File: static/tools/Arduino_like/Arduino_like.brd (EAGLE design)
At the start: 63.5 x 37.8 mm, 18 parts, among them IC1 MEGA8-P

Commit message: [Arduino_like] modify board.
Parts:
- moved C1-REGULATOR 1.91 mm to (8.26, 12.7)
- moved C2-REGULATOR 1.91 mm to (8.26, 27.9)
- moved IC2 1.91 mm to (4.45, 20.3)
- moved JP1 1.42 mm to (37.5, 34.3)
- moved CAVALIER_LED 1.27 mm to (55.9, 19.1)
- moved ALIM 0.64 mm to (4.45, 7.62)
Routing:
- net N$5: track 24.7 -> 27.5 mm
- net VCC: track 69.6 -> 67.7 mm
- net N$3: track 22.6 -> 24.2 mm
- net N$7: track 8.89 -> 10.4 mm
- net GND: track 146.4 -> 147.6 mm
- net N$4: track 53.9 -> 54.5 mm
- net N$26: track 3.07 -> 3.59 mm
- net N$6: track 9.42 -> 9.94 mm
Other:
- board size 63.5 x 37.8 mm -> 63.5 x 39 mm

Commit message: [Arduino_like] adds GND, VCC and AREF pins.
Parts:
- added JP6: (no value), pinhead:1X03
- moved CAVALIER_VCC 3.70 mm to (23.5, 36.2)
- moved JP1 2.54 mm to (37.5, 36.8)
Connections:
- new net N$29: IC1.21, JP6.1
- net GND: now also JP6.3
- net VCC: now also JP6.2
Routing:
- net N$29: track 0.00 -> 40.7 mm, vias 0 -> 1
- net VCC: track 67.7 -> 80.1 mm
- net GND: track 147.6 -> 158.2 mm
- net N$28: track 5.08 -> 12.7 mm
- net N$15: track 4.97 -> 8.41 mm
- net N$7: track 10.4 -> 13.0 mm
- net N$5: track 27.5 -> 30.0 mm
- net N$3: track 24.2 -> 26.7 mm
- net N$4: track 54.5 -> 57.1 mm
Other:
- board size 63.5 x 39 mm -> 62.2 x 42.9 mm
- board text added: "AREF"
- board text added: "GND"
- board text added: "VCC"

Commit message: [Arduino like] move on 0.1 inch grid.
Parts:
- moved CAVALIER_VCC 5.85 mm to (17.8, 37.5)
- moved JP1 5.72 mm to (31.8, 36.8)
- moved C1-REGULATOR 2.54 mm to (5.71, 12.7)
- moved C2-REGULATOR 2.54 mm to (5.71, 27.9)
- moved ALIM 2.54 mm to (1.91, 7.62)
- moved IC2 2.54 mm to (1.91, 20.3)
- moved C1-CRYSTAL 2.54 mm to (29.2, 7.62)
- moved C2-CRYSTAL 2.54 mm to (39.4, 7.62)
- moved CAVALIER_LED 2.54 mm to (53.3, 19.1)
- moved IC1 2.54 mm to (31.8, 19.1)
- moved JP2 2.54 mm to (21.6, 27.9)
- moved JP3 2.54 mm to (43.2, 27.9)
- moved JP4 2.54 mm to (20.3, 10.2)
- moved JP5 2.54 mm to (47.0, 10.2)
- moved LED1 2.54 mm to (57.1, 19.1)
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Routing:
- net N$34: track 0.00 -> 12.7 mm
- net N$31: track 0.00 -> 10.2 mm
- net N$40: track 0.00 -> 7.62 mm
- net N$32: track 0.00 -> 7.62 mm
- net N$37: track 0.00 -> 7.62 mm
- net N$35: track 0.00 -> 7.62 mm
- net N$30: track 0.00 -> 7.62 mm
- net N$41: track 0.00 -> 6.35 mm
- net N$38: track 0.00 -> 6.35 mm
- net N$36: track 0.00 -> 6.35 mm
- net N$33: track 0.00 -> 6.35 mm
- net N$39: track 0.00 -> 6.35 mm
- net GND: track 158.2 -> 163.1 mm
- net N$7: track 13.0 -> 14.3 mm
- net N$5: track 30.0 -> 31.3 mm
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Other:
- board size 62.2 x 42.9 mm -> 62.2 x 40.9 mm
- board text added: "BOTTOM"
- board text added: "TOP"
- board text added: "by Fab@ENAC-2015"

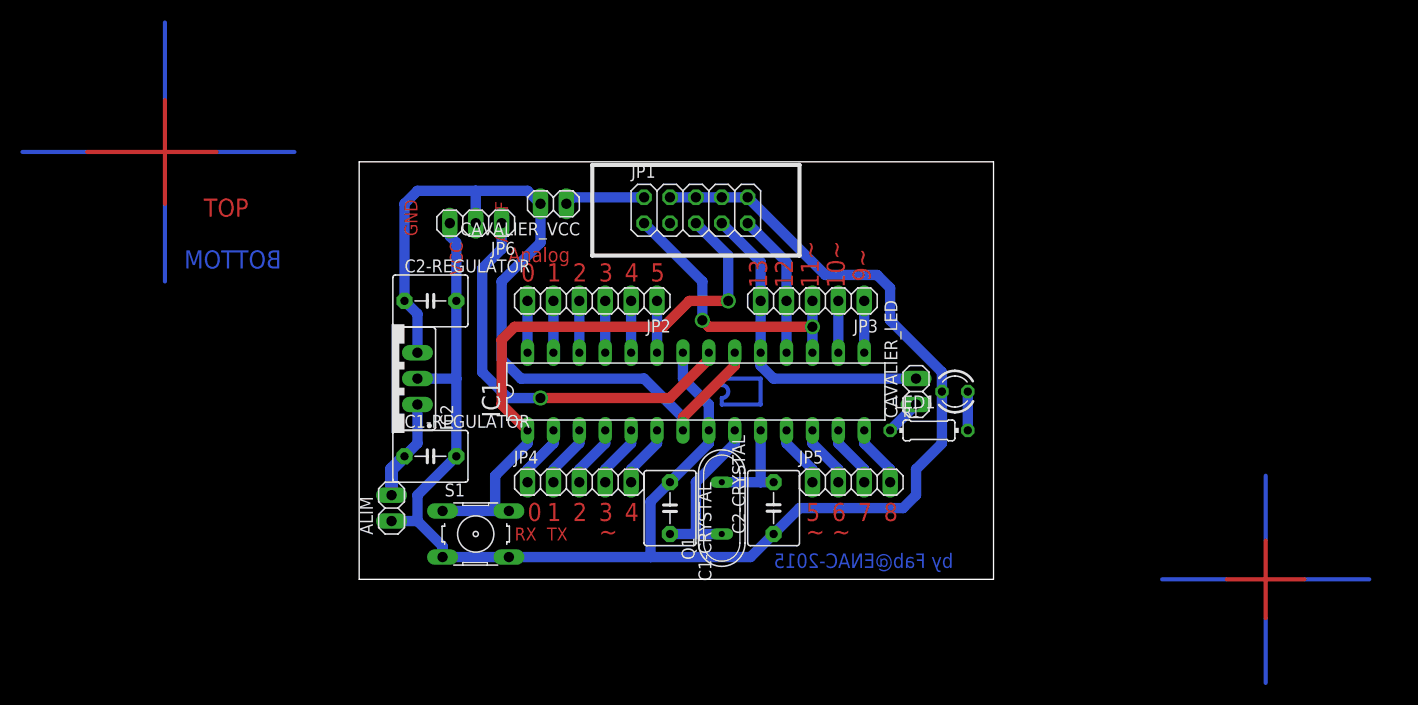
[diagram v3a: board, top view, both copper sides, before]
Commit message: [Arduino like] align pins.
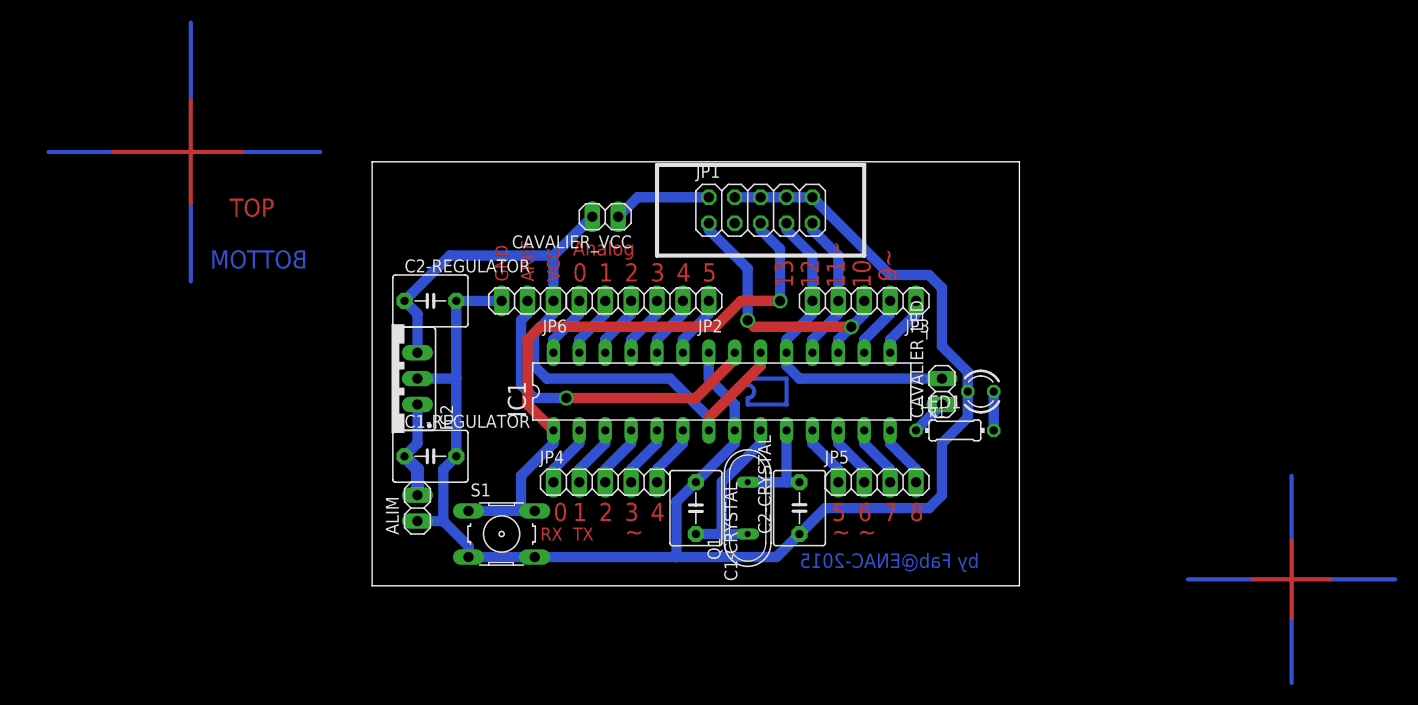
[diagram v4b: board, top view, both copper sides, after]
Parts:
- moved JP6 9.16 mm to (15.2, 27.9)
- moved JP1 6.35 mm to (38.1, 36.8)
- moved CAVALIER_VCC 5.24 mm to (22.9, 36.2)
- moved JP2 5.08 mm to (26.7, 27.9)
- moved JP3 5.08 mm to (48.3, 27.9)
- moved ALIM 2.54 mm to (4.45, 7.62)
- moved C1-CRYSTAL 2.54 mm to (31.8, 7.62)
- moved C2-CRYSTAL 2.54 mm to (41.9, 7.62)
- moved CAVALIER_LED 2.54 mm to (55.9, 19.1)
- moved IC1 2.54 mm to (34.3, 19.1)
- moved JP4 2.54 mm to (22.9, 10.2)
- moved JP5 2.54 mm to (49.5, 10.2)
- moved LED1 2.54 mm to (59.7, 19.1)
- moved Q1 2.54 mm to (36.8, 7.62)
- moved R1 2.54 mm to (57.1, 15.2)
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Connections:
- removed net N$29: IC1.21, JP6.1
- new net AREF: IC1.21, JP6.2
- net VCC: now also JP6.1; no longer JP6.2
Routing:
- net N$29: track 40.9 -> 0.00 mm, vias 1 -> 0
- net AREF: track 0.00 -> 32.2 mm, vias 0 -> 1
- net VCC: track 80.7 -> 69.3 mm
- net GND: track 163.1 -> 156.3 mm
- net N$4: track 58.4 -> 60.4 mm
- net N$15: track 7.88 -> 9.68 mm
- net N$24: track 5.08 -> 6.13 mm
- net N$8: track 5.08 -> 6.13 mm
- net N$10: track 5.08 -> 6.13 mm
- net N$9: track 5.08 -> 6.13 mm
- net N$25: track 5.08 -> 6.13 mm
- net N$13: track 5.08 -> 6.13 mm
- net N$12: track 5.08 -> 6.13 mm
- net N$11: track 5.08 -> 6.13 mm
- net N$7: track 14.3 -> 14.8 mm
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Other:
- board size 62.2 x 40.9 mm -> 63.5 x 41.6 mm

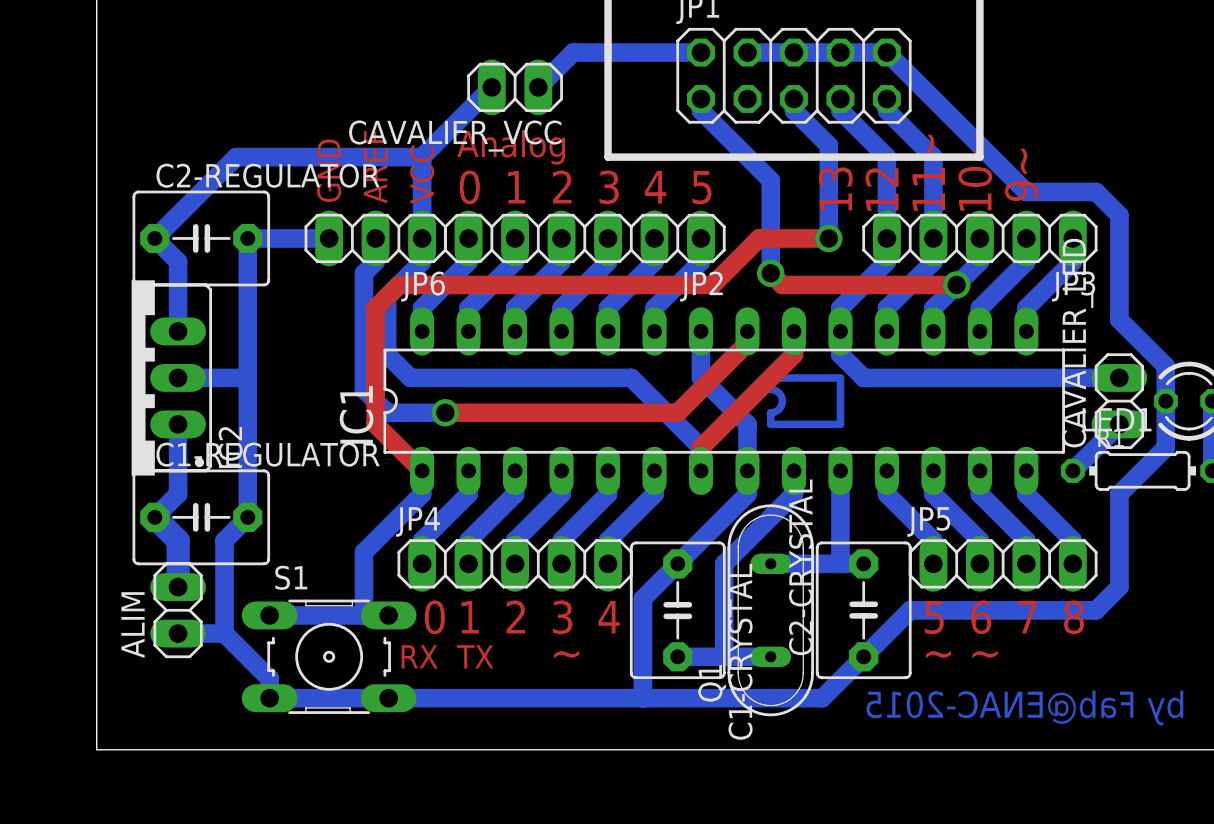
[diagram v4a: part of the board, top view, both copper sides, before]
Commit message: [Arduino_like] align power.
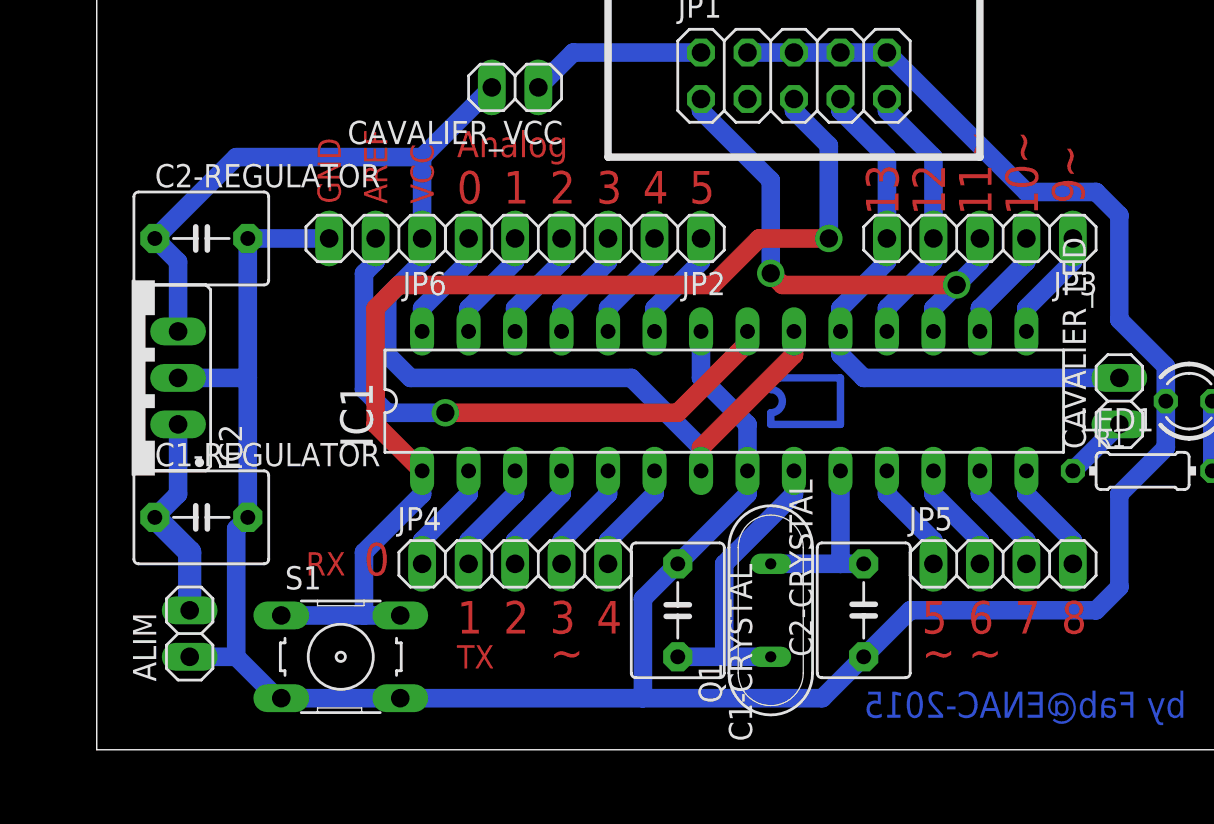
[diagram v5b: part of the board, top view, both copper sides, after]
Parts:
- moved ALIM 1.42 mm to (5.08, 6.35)
- moved S1 0.64 mm to (13.3, 5.08)
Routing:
- net N$6: track 9.94 -> 11.5 mm
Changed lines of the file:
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@@
 <layer number="19" name="Unrouted" color="6" fill="1" visible="yes" active="yes"/>
 <layer number="20" name="Dimension" color="15" fill="1" visible="yes" active="yes"/>
-<layer number="21" name="tPlace" color="7" fill="1" visible="yes" active="yes"/>
-<layer number="22" name="bPlace" color="7" fill="1" visible="yes" active="yes"/>
+<layer number="21" name="tPlace" color="7" fill="1" visible="no" active="yes"/>
+<layer number="22" name="bPlace" color="7" fill="1" visible="no" active="yes"/>
 <layer number="23" name="tOrigins" color="15" fill="1" visible="no" active="yes"/>
 <layer number="24" name="bOrigins" color="15" fill="1" visible="no" active="yes"/>
@@
 <wire x1="63.48" y1="41.58" x2="0" y2="41.58" width="0" layer="20"/>
 <wire x1="0" y1="41.58" x2="0" y2="0" width="0" layer="20"/>
-<text x="17.78" y="6.35" size="1.778" layer="1">0</text>
+<text x="14.605" y="9.525" size="1.778" layer="1">0</text>
 <text x="19.685" y="6.35" size="1.778" layer="1">1</text>
 <text x="22.225" y="6.35" size="1.778" layer="1">2</text>
@@
 <text x="50.165" y="6.35" size="1.778" layer="1">7</text>
 <text x="52.705" y="6.35" size="1.778" layer="1">8</text>
-<text x="51.435" y="29.845" size="1.778" layer="1" rot="R90">9~</text>
-<text x="48.895" y="29.21" size="1.778" layer="1" rot="R90">10~</text>
-<text x="46.355" y="29.21" size="1.778" layer="1" rot="R90">11~</text>
-<text x="43.815" y="29.21" size="1.778" layer="1" rot="R90">12</text>
-<text x="41.275" y="29.21" size="1.778" layer="1" rot="R90">13</text>
+<text x="53.975" y="29.845" size="1.778" layer="1" rot="R90">9~</text>
+<text x="51.435" y="29.21" size="1.778" layer="1" rot="R90">10~</text>
+<text x="48.895" y="29.21" size="1.778" layer="1" rot="R90">11~</text>
+<text x="46.355" y="29.21" size="1.778" layer="1" rot="R90">12</text>
+<text x="43.815" y="29.21" size="1.778" layer="1" rot="R90">13</text>
 <text x="19.685" y="29.845" size="1.778" layer="1">0</text>
 <text x="22.225" y="29.845" size="1.778" layer="1">1</text>
@@
 <text x="47.625" y="4.445" size="1.778" layer="1">~</text>
 <text x="19.685" y="4.445" size="1.27" layer="1">TX</text>
-<text x="16.51" y="4.445" size="1.27" layer="1">RX</text>
+<text x="11.43" y="9.525" size="1.27" layer="1">RX</text>
 <wire x1="27.94" y1="41.275" x2="27.94" y2="32.385" width="0.4064" layer="21"/>
 <wire x1="27.94" y1="41.275" x2="48.26" y2="41.275" width="0.4064" layer="21"/>
@@
 <text x="-13.97" y="36.195" size="1.778" layer="1">TOP</text>
 <text x="-6.35" y="31.115" size="1.778" layer="16" rot="MR0">BOTTOM</text>
+<dimension x1="27.94" y1="10.16" x2="45.72" y2="10.16" x3="36.83" y3="-15.24" layer="47"/>
+<dimension x1="53.34" y1="10.16" x2="53.34" y2="27.94" x3="78.74" y3="19.05" layer="47"/>
+<dimension x1="43.18" y1="27.94" x2="33.02" y2="27.94" x3="38.1" y3="48.26" layer="47"/>
 </plain>
 <attributes>
@@
 <element name="C1-REGULATOR" library="capacitor-wima" package="C5B5" value="" x="5.715" y="12.7"/>
 <element name="C2-REGULATOR" library="capacitor-wima" package="C5B5" value="" x="5.715" y="27.94"/>
-<element name="ALIM" library="pinhead" package="1X02" value="" x="4.445" y="7.62" rot="R90"/>
+<element name="ALIM" library="pinhead" package="1X02" value="" x="5.08" y="6.35" rot="R90"/>
 <element name="JP1" library="pinhead" package="2X05" value="" x="38.1" y="36.83"/>
 <element name="CAVALIER_VCC" library="pinhead" package="1X02" value="" x="22.86" y="36.195" rot="R180"/>
@@
 <element name="R1" library="rcl" package="0204/7" value="" x="57.15" y="15.24"/>
 <element name="LED1" library="led" package="LED3MM" value="" x="59.69" y="19.05" rot="R180"/>
-<element name="S1" library="switch-omron" package="B3F-10XX" value="" x="12.7" y="5.08">
-<attribute name="OC_NEWARK" value="36M3542" x="12.7" y="5.08" size="1.778" layer="27" display="off"/>
-<attribute name="MPN" value="B3F-1000" x="12.7" y="5.08" size="1.778" layer="27" display="off"/>
-<attribute name="MF" value="" x="12.7" y="5.08" size="1.778" layer="27" display="off"/>
-<attribute name="OC_FARNELL" value="176432" x="12.7" y="5.08" size="1.778" layer="27" display="off"/>
+<element name="S1" library="switch-omron" package="B3F-10XX" value="" x="13.335" y="5.08">
+<attribute name="OC_NEWARK" value="36M3542" x="13.335" y="5.08" size="1.778" layer="27" display="off"/>
+<attribute name="MPN" value="B3F-1000" x="13.335" y="5.08" size="1.778" layer="27" display="off"/>
+<attribute name="MF" value="" x="13.335" y="5.08" size="1.778" layer="27" display="off"/>
+<attribute name="OC_FARNELL" value="176432" x="13.335" y="5.08" size="1.778" layer="27" display="off"/>
 </element>
 <element name="JP4" library="pinhead" package="1X05" value="" x="22.86" y="10.16"/>
@@
 <wire x1="4.445" y1="17.78" x2="4.445" y2="13.97" width="1.016" layer="16"/>
 <wire x1="4.445" y1="13.97" x2="3.175" y2="12.7" width="1.016" layer="16"/>
-<wire x1="4.445" y1="8.89" x2="4.445" y2="11.43" width="1.27" layer="16"/>
-<wire x1="4.445" y1="11.43" x2="3.175" y2="12.7" width="1.27" layer="16"/>
+<wire x1="5.08" y1="7.62" x2="5.08" y2="10.795" width="1.27" layer="16"/>
+<wire x1="5.08" y1="10.795" x2="3.175" y2="12.7" width="1.27" layer="16"/>
 </signal>
 <signal name="N$4">
@@
 <wire x1="15.24" y1="17.78" x2="17.78" y2="15.24" width="1.016" layer="1"/>
 <contactref element="S1" pad="2"/>
-<wire x1="9.4488" y1="7.3406" x2="14.605" y2="7.3406" width="1.016" layer="16"/>
-<wire x1="14.605" y1="7.3406" x2="15.9512" y2="7.3406" width="1.016" layer="16"/>
+<wire x1="10.0838" y1="7.3406" x2="14.605" y2="7.3406" width="1.016" layer="16"/>
+<wire x1="14.605" y1="7.3406" x2="16.5862" y2="7.3406" width="1.016" layer="16"/>
 <wire x1="17.78" y1="15.24" x2="17.78" y2="13.97" width="1.016" layer="16"/>
 <wire x1="17.78" y1="13.97" x2="14.605" y2="10.795" width="1.016" layer="16"/>
@@
 <wire x1="8.255" y1="20.32" x2="8.255" y2="12.7" width="1.016" layer="16"/>
 <wire x1="4.445" y1="20.32" x2="8.255" y2="20.32" width="1.016" layer="16"/>
-<wire x1="9.4488" y1="2.8194" x2="15.9512" y2="2.8194" width="1.016" layer="16"/>
-<wire x1="8.255" y1="12.7" x2="6.985" y2="11.43" width="1.016" layer="16"/>
-<wire x1="6.985" y1="11.43" x2="6.985" y2="6.35" width="1.016" layer="16"/>
-<wire x1="6.985" y1="6.35" x2="4.445" y2="6.35" width="1.016" layer="16"/>
+<wire x1="10.0838" y1="2.8194" x2="16.5862" y2="2.8194" width="1.016" layer="16"/>
+<wire x1="8.255" y1="12.7" x2="7.62" y2="12.065" width="1.016" layer="16"/>
+<wire x1="7.62" y1="12.065" x2="7.62" y2="5.08" width="1.016" layer="16"/>
+<wire x1="7.62" y1="5.08" x2="5.08" y2="5.08" width="1.016" layer="16"/>
 <wire x1="58.42" y1="19.05" x2="58.42" y2="16.51" width="1.016" layer="16"/>
 <wire x1="58.42" y1="16.51" x2="55.88" y2="13.97" width="1.016" layer="16"/>
@@
 <wire x1="44.45" y1="7.62" x2="41.91" y2="5.08" width="1.016" layer="16"/>
 <wire x1="58.42" y1="19.05" x2="58.42" y2="20.955" width="1.016" layer="16"/>
-<wire x1="9.4488" y1="2.8194" x2="9.4488" y2="3.8862" width="1.016" layer="16"/>
-<wire x1="9.4488" y1="3.8862" x2="6.985" y2="6.35" width="1.016" layer="16"/>
+<wire x1="10.0838" y1="2.8194" x2="10.0838" y2="2.6162" width="1.016" layer="16"/>
+<wire x1="10.0838" y1="2.6162" x2="7.62" y2="5.08" width="1.016" layer="16"/>
 <contactref element="JP6" pad="3"/>
-<wire x1="15.9512" y1="2.8194" x2="29.845" y2="2.8194" width="1.016" layer="16"/>
+<wire x1="16.5862" y1="2.8194" x2="29.845" y2="2.8194" width="1.016" layer="16"/>
 <wire x1="29.845" y1="2.8194" x2="39.6494" y2="2.8194" width="1.016" layer="16"/>
 <wire x1="39.6494" y1="2.8194" x2="41.91" y2="5.08" width="1.016" layer="16"/>
@@
 </signal>
 </signals>
-<errors>
-</errors>
 </board>
 </drawing>
